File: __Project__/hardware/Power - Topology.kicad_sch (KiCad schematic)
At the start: 0 parts

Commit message: Update project template
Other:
- company: (none) -> ${COMPANY}
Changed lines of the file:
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@@
 	(generator_version "9.0")
 	(paper "A3")
+	(title_block
+		(date "2025-06-05")
+		(rev "${REVISION}")
+		(company "${COMPANY}")
+	)
 	(rectangle
-		(start 335.28 250.19)
-		(end 406.4 250.952)
+		(start 334.01 240.03)
+		(end 405.13 240.792)
 		(stroke
 			(width 0)
@@
 	)
 	(rectangle
-		(start 335.28 217.17)
-		(end 406.4 217.932)
+		(start 334.01 207.01)
+		(end 405.13 207.772)
 		(stroke
 			(width 0)
@@
 	(text_box "Spec 2"
 		(exclude_from_sim no)
-		(at 336.55 226.06 0)
+		(at 335.28 215.9 0)
 		(size 43.18 7.62)
 		(margins 2.2859 2.2859 2.2859 2.2859)
@@
 	(text_box "Input voltage:"
 		(exclude_from_sim no)
-		(at 336.55 218.44 0)
+		(at 335.28 208.28 0)
 		(size 41.91 7.62)
 		(margins 2.2859 2.2859 2.2859 2.2859)
@@
 	(text_box "Spec 4"
 		(exclude_from_sim no)
-		(at 336.55 241.3 0)
+		(at 335.28 231.14 0)
 		(size 44.45 7.62)
 		(margins 2.2859 2.2859 2.2859 2.2859)
@@
 	(text_box "?? - ?? V"
 		(exclude_from_sim no)
-		(at 382.27 218.44 0)
+		(at 381 208.28 0)
 		(size 24.13 7.62)
 		(margins 2.2859 2.2859 2.2859 2.2859)
@@
 	(text_box "Target specifications:"
 		(exclude_from_sim no)
-		(at 332.74 209.55 0)
+		(at 331.47 199.39 0)
 		(size 73.66 7.62)
 		(margins 2.2859 2.2859 2.2859 2.2859)
@@
 	(text_box "??"
 		(exclude_from_sim no)
-		(at 382.27 241.3 0)
+		(at 381 231.14 0)
 		(size 24.13 7.62)
 		(margins 2.2859 2.2859 2.2859 2.2859)
@@
 	(text_box "??"
 		(exclude_from_sim no)
-		(at 382.27 233.68 0)
+		(at 381 223.52 0)
 		(size 24.13 7.62)
 		(margins 2.2859 2.2859 2.2859 2.2859)
@@
 	(text_box "Spec 3"
 		(exclude_from_sim no)
-		(at 336.55 233.68 0)
+		(at 335.28 223.52 0)
 		(size 41.91 7.62)
 		(margins 2.2859 2.2859 2.2859 2.2859)
@@
 	(text_box "??"
 		(exclude_from_sim no)
-		(at 382.27 226.06 0)
-		(size 24.13 7.62)
-		(margins 2.2859 2.2859 2.2859 2.2859)
+		(at 381 215.9 0)
+		(size 24.13 7.62)
+		(margins 2.2859 2.2859 2.2859 2.2859)

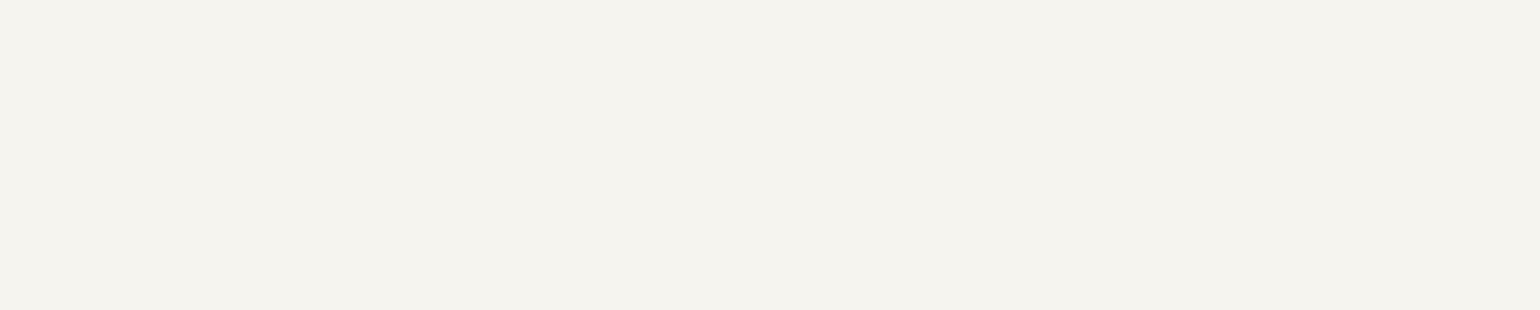
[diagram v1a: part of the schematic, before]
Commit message: Fix JST footprints
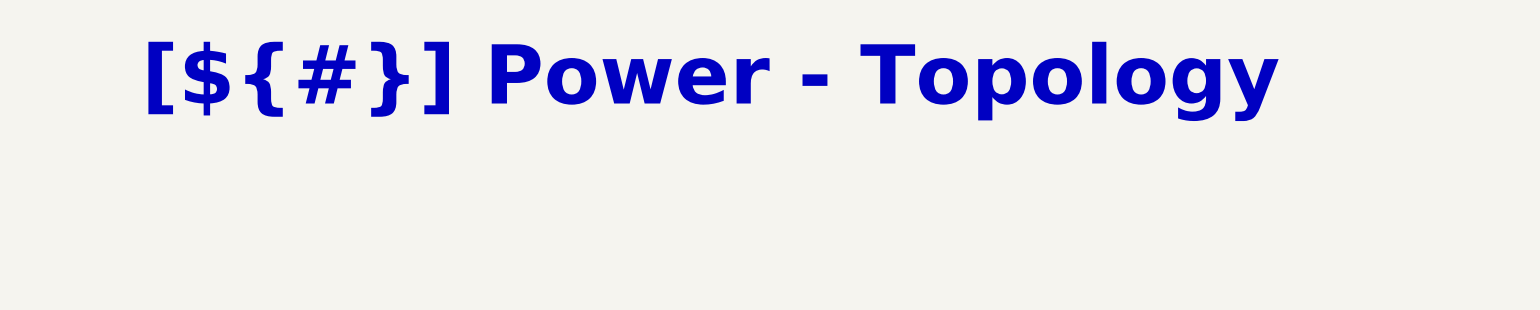
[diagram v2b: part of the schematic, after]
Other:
- title: (none) -> Power - Topology
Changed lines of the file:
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@@
 	(paper "A3")
 	(title_block
+		(title "Power - Topology")
 		(date "2025-06-05")
 		(rev "${REVISION}")
@@
 		)
 	)
+	(text_box "[${#}] ${TITLE}"
+		(exclude_from_sim no)
+		(at 12.7 12.7 0)
+		(size 394.97 20.32)
+		(margins 5.9999 5.9999 5.9999 5.9999)
+		(stroke
+			(width -0.0001)
+			(type default)
+		)
+		(fill
+			(type none)
+		)
+		(effects
+			(font
+				(face "Times New Roman")
+				(size 8 8)
+				(thickness 1.2)
+				(bold yes)
+				(color 162 22 34 1)
+			)
+		)
+	)
